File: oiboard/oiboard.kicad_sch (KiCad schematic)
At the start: 37 parts, among them J1 Conn_01x04, U1 LM324

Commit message: feat: finalize the board layout
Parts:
- removed D?: (no value), symbol LED:WS2812
- added D1, D10, D11, D12, D13, D14, D15, D16, D2, D3, D4, D5, D6, D7, D8, D9: APA102, LED_SMD:LED_RGB_5050-6, symbol LED:APA102
- added TP1, TP10, TP11, TP12, TP13, TP2, TP3, TP4, TP5, TP6, TP7, TP8, TP9: TestPoint, TestPoint:TestPoint_THTPad_D1.5mm_Drill0.7mm, symbol Connector:TestPoint
- D17: renamed from D?; value (none) -> LED; footprint (none) -> LED_THT:LED_D5.0mm
- D18, D19, D20: renamed from D?; footprint (none) -> LED_THT:LED_D5.0mm
- Q1: renamed from Q?; value (none) -> 2N3904; footprint (none) -> Package_TO_SOT_THT:TO-92_Inline
- R1: footprint Resistor_THT:R_Axial_DIN0207_L6.3mm_D2.5mm_P15.24mm_Horizontal -> Resistor_THT:R_Axial_DIN0207_L6.3mm_D2.5mm_P10.16mm_Horizontal
- R10, R8, R9: renamed from R?; value R -> 10k; footprint (none) -> Resistor_THT:R_Axial_DIN0207_L6.3mm_D2.5mm_P10.16mm_Horizontal
- R11, R12, R13, R15, R2, R3, R4, R5, R6, R7: renamed from R?; footprint Resistor_THT:R_Axial_DIN0207_L6.3mm_D2.5mm_P15.24mm_Horizontal -> Resistor_THT:R_Axial_DIN0207_L6.3mm_D2.5mm_P10.16mm_Horizontal
- R14: renamed from R?; footprint Resistor_THT:R_Axial_DIN0207_L6.3mm_D2.5mm_P15.24mm_Horizontal -> Button_Switch_THT:SW_CuK_JS202011CQN_DPDT_Straight
- SW1: renamed from SW?; footprint (none) -> Button_Switch_THT:SW_PUSH_6mm
- SW2: renamed from SW?; footprint (none) -> Button_Switch_THT:SW_DIP_SPSTx03_Slide_9.78x9.8mm_W7.62mm_P2.54mm
- gave numbers to parts that had none: 10
- renumbered J1 to J3
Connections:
- net GND is gone; now on net +5V: A1.29 (GND), A1.4 (GND), J1.1 (Pin_1), J1.4 (Pin_4), J2.1 (Pin_1), J2.4 (Pin_4), J3.1 (Pin_1), J4.1 (Pin_1), J5.1 (Pin_1), J7.1 (Pin_1), Q1.1 (E), Q2.1 (E), Q3.1 (E), Q4.1 (E), R10.2, R11.2, R2.1, R4.2, R6.2, R8.2, R9.2, SW1.1, U1.11 (V-)
- net +5V: now also D1.3 (GND), D1.4 (VCC), D10.3 (GND), D10.4 (VCC), D11.3 (GND), D11.4 (VCC), D12.3 (GND), D12.4 (VCC), D13.3 (GND), D13.4 (VCC), D14.3 (GND), D14.4 (VCC), D15.3 (GND), D15.4 (VCC), D16.3 (GND), D16.4 (VCC), D2.3 (GND), D2.4 (VCC), D3.3 (GND), D3.4 (VCC), D4.3 (GND), D4.4 (VCC), D5.3 (GND), D5.4 (VCC), D6.3 (GND), D6.4 (VCC), D7.3 (GND), D7.4 (VCC), D8.3 (GND), D8.4 (VCC), D9.3 (GND), D9.4 (VCC)
- net led_a: now also TP10.1
- net led_b: now also TP11.1
- net led_c: now also TP12.1
- net led_d: now also TP13.1
- net sensor_a: now also TP1.1
- net sensor_b: now also TP2.1
- net sensor_c: now also TP3.1
- net sensor_d: now also TP9.1
- net sw3: now reaches R10.1, SW2.4
- net sw3: now also A1.21 (A2), TP7.1
- net led_data: now reaches A1.10 (D7)
- net led_data: now also D8.1 (DI), TP6.1
- net led_clock : now reaches A1.11 (D8)
- net led_clock : now also D8.2 (CI), TP8.1
- net sw1: now reaches A1.19 (A0)
- net sw1: now also R8.1, SW2.6, TP4.1
- net sw2: now reaches A1.20 (A1)
- net sw2: now also R9.1, SW2.5, TP5.1
- new net: D12.6 (DO), D13.1 (DI)
- new net: D12.5 (CO), D13.2 (CI)
- new net: D13.5 (CO), D14.2 (CI)
- new net: D13.6 (DO), D14.1 (DI)
- new net: D6.1 (DI), D7.6 (DO)
- new net: D6.2 (CI), D7.5 (CO)
- new net: D5.2 (CI), D6.5 (CO)
- new net: D5.1 (DI), D6.6 (DO)
- new net: D14.6 (DO), D15.1 (DI)
- new net: D14.5 (CO), D15.2 (CI)
- new net: D15.5 (CO), D16.2 (CI)
- new net: D15.6 (DO), D16.1 (DI)
- new net: D7.2 (CI), D8.5 (CO)
- new net: D7.1 (DI), D8.6 (DO)
- new net: D11.6 (DO), D12.1 (DI)
- new net: D11.5 (CO), D12.2 (CI)
- new net: D1.6 (DO), D9.1 (DI)
- new net: D1.5 (CO), D9.2 (CI)
- new net: D10.2 (CI), D9.5 (CO)
- new net: D10.1 (DI), D9.6 (DO)
- new net: D2.1 (DI), D3.6 (DO)
- new net: D2.2 (CI), D3.5 (CO)
- new net: D1.2 (CI), D2.5 (CO)
- new net: D1.1 (DI), D2.6 (DO)
- new net: D4.1 (DI), D5.6 (DO)
- new net: D4.2 (CI), D5.5 (CO)
- new net: D3.2 (CI), D4.5 (CO)
- new net: D3.1 (DI), D4.6 (DO)
- new net: D10.6 (DO), D11.1 (DI)
- new net: D10.5 (CO), D11.2 (CI)
- no-connect marks 5 -> 11
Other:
- moved on the sheet: A1, D17, D18, D19, D20, J3, J4, J5, J6, J7, Q1, Q2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

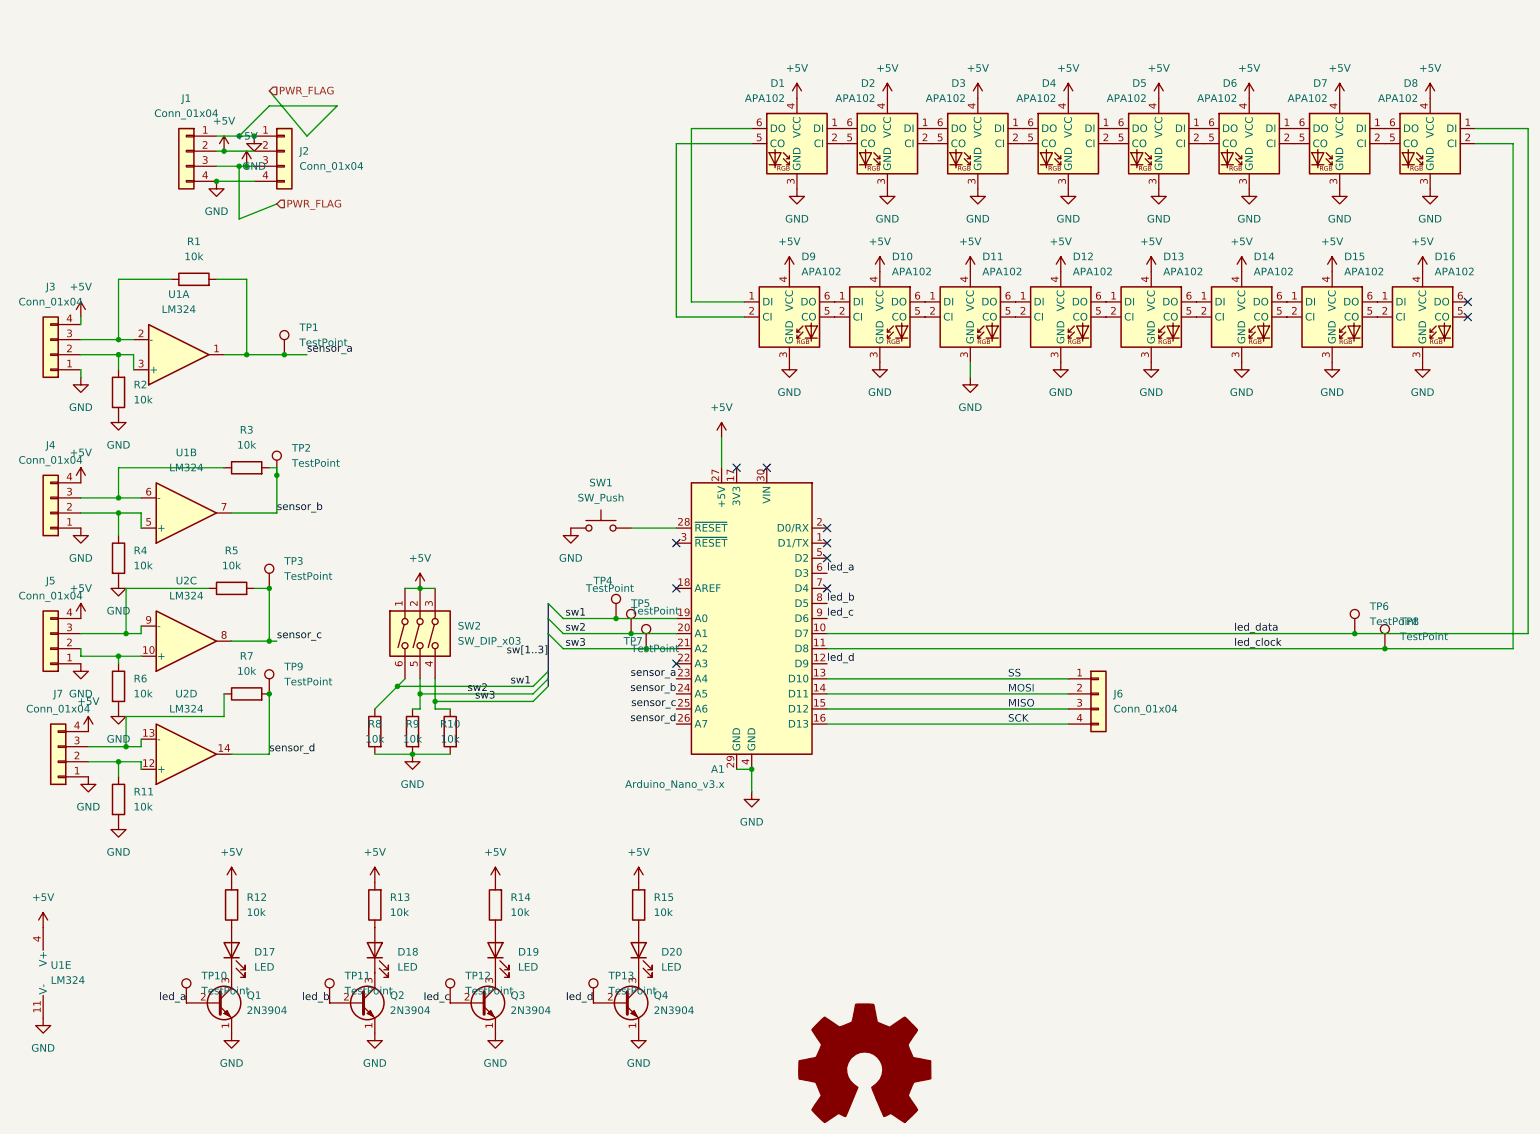
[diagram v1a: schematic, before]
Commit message: add premlimarp PCB layout
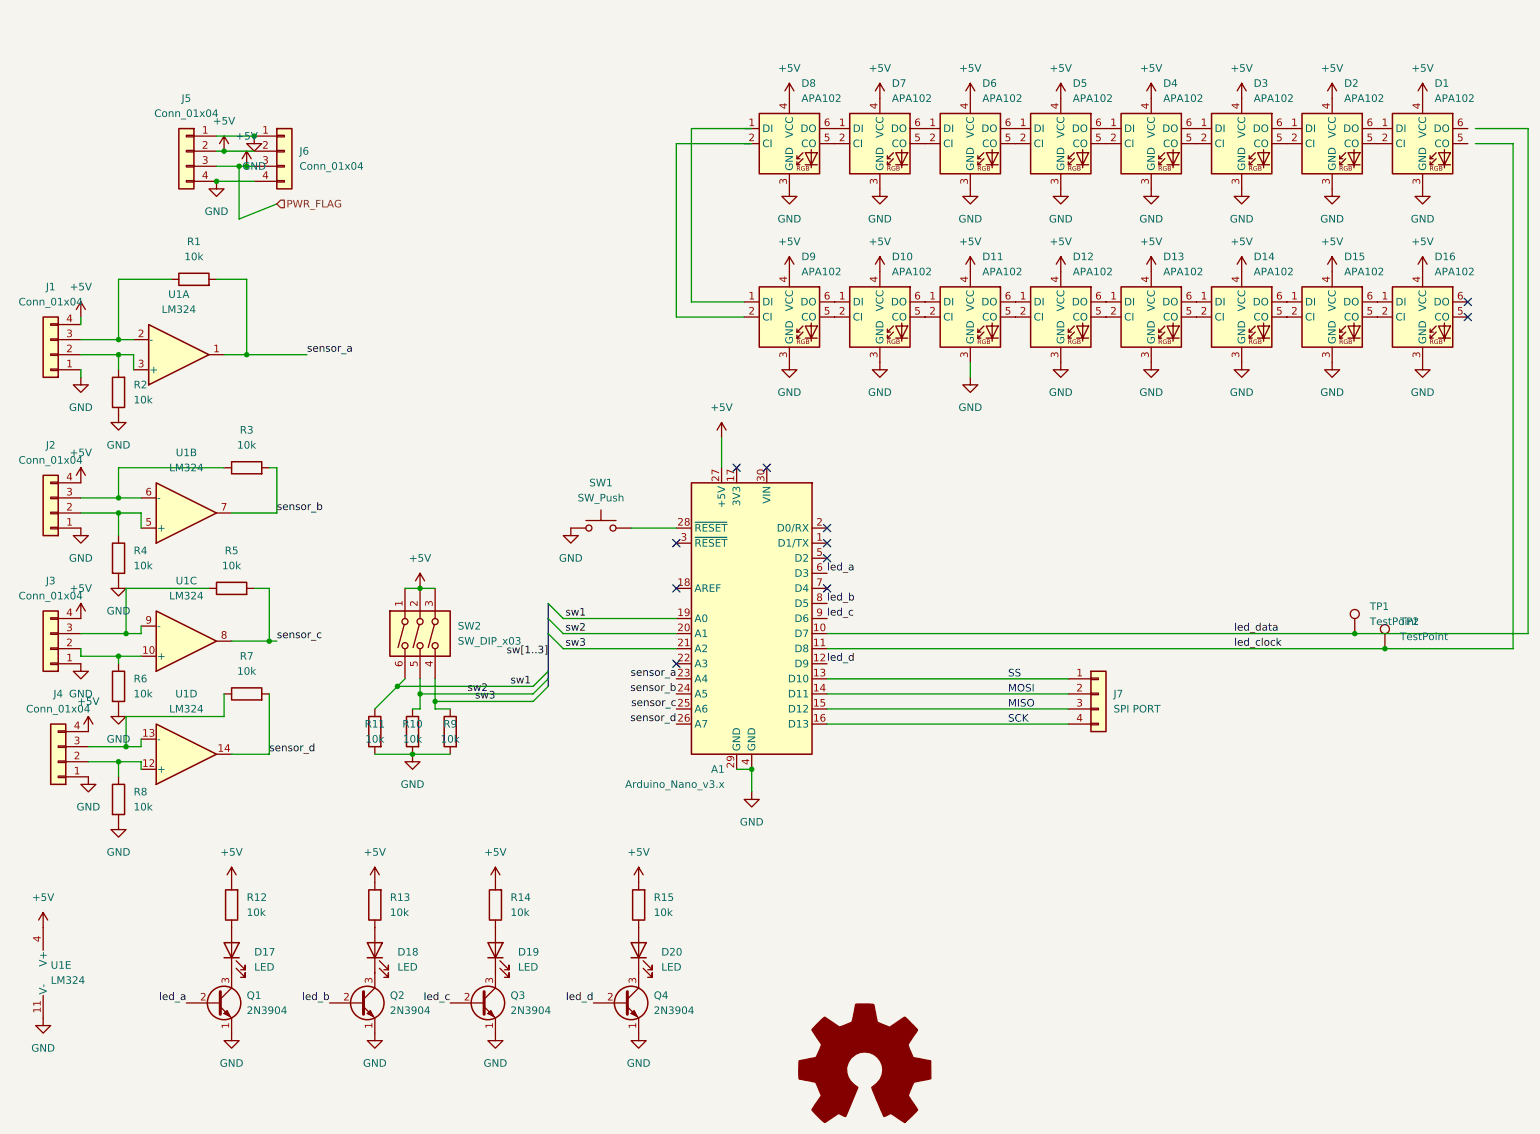
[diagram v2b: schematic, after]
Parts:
- removed TP1, TP10, TP11, TP12, TP13, TP2, TP3, TP4, TP5, TP7, TP9: TestPoint, TestPoint:TestPoint_THTPad_D1.5mm_Drill0.7mm, symbol Connector:TestPoint
- J7: renamed from J6; value Conn_01x04 -> SPI PORT; footprint TerminalBlock:TerminalBlock_bornier-4_P5.08mm -> Connector_PinHeader_2.54mm:PinHeader_1x04_P2.54mm_Horizontal
- R14: footprint Button_Switch_THT:SW_CuK_JS202011CQN_DPDT_Straight -> Resistor_THT:R_Axial_DIN0207_L6.3mm_D2.5mm_P10.16mm_Horizontal
- renumbered J3 to J1, J4 to J2, J5 to J3, J7 to J4, J1 to J5, J2 to J6, R9 to R10, R8 to R11, R11 to R8, R10 to R9, TP6 to TP1, TP8 to TP2, U2 to U1
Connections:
- net +5V: no longer A1.29 (GND), A1.4 (GND), D1.3 (GND), D10.3 (GND), D11.3 (GND), D12.3 (GND), D13.3 (GND), D14.3 (GND), D15.3 (GND), D16.3 (GND), D2.3 (GND), D3.3 (GND), D4.3 (GND), D5.3 (GND), D6.3 (GND), D7.3 (GND), D8.3 (GND), D9.3 (GND), J1.1 (Pin_1), J2.1 (Pin_1), J3.1 (Pin_1), J4.1 (Pin_1), J5.1 (Pin_1), J5.4 (Pin_4), J6.1 (Pin_1), J6.4 (Pin_4), Q1.1 (E), Q2.1 (E), Q3.1 (E), Q4.1 (E), R10.2, R11.2, R2.1, R4.2, R6.2, R8.2, R9.2, SW1.1, U1.11 (V-)
- net led_clock : no longer D8.2 (CI)
- net led_data: no longer D8.1 (DI)
- net at D9.1 (DI): no longer D1.6 (DO)
- net at D9.2 (CI): no longer D1.5 (CO)
- new net GND: A1.29 (GND), A1.4 (GND), D1.3 (GND), D10.3 (GND), D11.3 (GND), D12.3 (GND), D13.3 (GND), D14.3 (GND), D15.3 (GND), D16.3 (GND), D2.3 (GND), D3.3 (GND), D4.3 (GND), D5.3 (GND), D6.3 (GND), D7.3 (GND), D8.3 (GND), D9.3 (GND), J1.1 (Pin_1), J2.1 (Pin_1), J3.1 (Pin_1), J4.1 (Pin_1), J5.1 (Pin_1), J5.4 (Pin_4), J6.1 (Pin_1), J6.4 (Pin_4), Q1.1 (E), Q2.1 (E), Q3.1 (E), Q4.1 (E), R10.2, R11.2, R2.1, R4.2, R6.2, R8.2, R9.2, SW1.1, U1.11 (V-)
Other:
- moved on the sheet: D1, D2, D3, D4, D5, D6, D7, D8

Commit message: finalize pcb design 0.0
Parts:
- removed TP1, TP2: TestPoint, TestPoint:TestPoint_THTPad_D1.5mm_Drill0.7mm, symbol Connector:TestPoint
- added H1, H2, H3, H4: (no value), symbol Mechanical:MountingHole
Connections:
- net led_clock : now also D1.5 (CO)
- net led_data: now also D1.6 (DO)
- net sensor_b: now also A1.26 (A7); no longer A1.24 (A5)
- net sensor_c: now also A1.24 (A5), U1.14; no longer A1.25 (A6), U1.8
- net sensor_d: now also A1.25 (A6), U1.8; no longer A1.26 (A7), U1.14
- net at R3.1, U1.6 (-): now also J4.3 (Pin_3); no longer J2.3 (Pin_3)
- net at J3.2 (Pin_2), U1.10 (+): now also R8.1; no longer R6.1
- net at R4.1, U1.5 (+): now also J4.2 (Pin_2); no longer J2.2 (Pin_2)
- net at R1.1, U1.2 (-): now also J2.3 (Pin_3); no longer J1.3 (Pin_3)
- net at D8.1 (DI): now also D9.1 (DI)
- net at D8.2 (CI): now also D9.2 (CI)
- net at R2.2, U1.3 (+): now also J2.2 (Pin_2); no longer J1.2 (Pin_2)
- net at J3.3 (Pin_3), U1.9 (-): now also R7.1; no longer R5.1
- new net: J1.2 (Pin_2), R6.1, U1.12 (+)
- new net: J1.3 (Pin_3), R5.1, U1.13 (-)
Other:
- moved on the sheet: J1, J2, J3, J4, J7, U1C, U1D

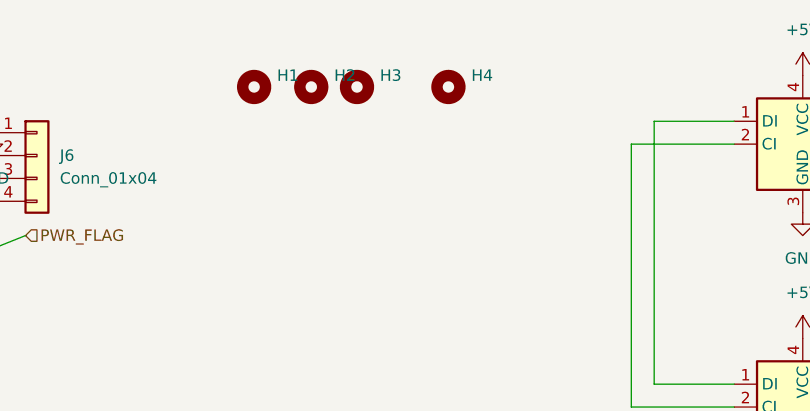
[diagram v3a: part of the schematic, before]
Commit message: add logo to board
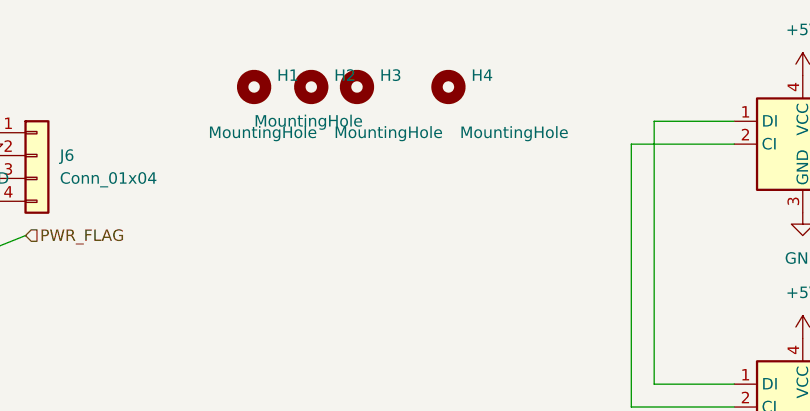
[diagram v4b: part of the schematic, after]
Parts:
- H1, H2, H3, H4: value (none) -> MountingHole; footprint (none) -> MountingHole:MountingHole_3mm
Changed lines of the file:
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@@
       (effects (font (size 1.27 1.27)) (justify left))
     )
-    (property "Value" "" (id 1) (at 88.9 26.67 0)
-      (effects (font (size 1.27 1.27)) (justify left))
-    )
-    (property "Footprint" "" (id 2) (at 95.25 22.86 0)
+    (property "Value" "MountingHole" (id 1) (at 88.9 26.67 0)
+      (effects (font (size 1.27 1.27)) (justify left))
+    )
+    (property "Footprint" "MountingHole:MountingHole_3mm" (id 2) (at 95.25 22.86 0)
       (effects (font (size 1.27 1.27)) hide)
     )
@@
       (effects (font (size 1.27 1.27)) (justify left))
     )
-    (property "Value" "" (id 1) (at 83.82 27.94 0)
-      (effects (font (size 1.27 1.27)) (justify left))
-    )
-    (property "Footprint" "" (id 2) (at 88.9 22.86 0)
+    (property "Value" "MountingHole" (id 1) (at 83.82 27.94 0)
+      (effects (font (size 1.27 1.27)) (justify left))
+    )
+    (property "Footprint" "MountingHole:MountingHole_3mm" (id 2) (at 88.9 22.86 0)
       (effects (font (size 1.27 1.27)) hide)
     )
@@
       (effects (font (size 1.27 1.27)) (justify left))
     )
-    (property "Value" "" (id 1) (at 97.79 27.94 0)
-      (effects (font (size 1.27 1.27)) (justify left))
-    )
-    (property "Footprint" "" (id 2) (at 100.33 22.86 0)
+    (property "Value" "MountingHole" (id 1) (at 97.79 27.94 0)
+      (effects (font (size 1.27 1.27)) (justify left))
+    )
+    (property "Footprint" "MountingHole:MountingHole_3mm" (id 2) (at 100.33 22.86 0)
       (effects (font (size 1.27 1.27)) hide)
     )
@@
       (effects (font (size 1.27 1.27)) (justify left))
     )
-    (property "Value" "" (id 1) (at 111.76 27.94 0)
-      (effects (font (size 1.27 1.27)) (justify left))
-    )
-    (property "Footprint" "" (id 2) (at 110.49 22.86 0)
-      (effects (font (size 1.27 1.27)) hide)
-    )
+    (property "Value" "MountingHole" (id 1) (at 111.76 27.94 0)
+      (effects (font (size 1.27 1.27)) (justify left))
+    )
+    (property "Footprint" "MountingHole:MountingHole_3mm" (id 2) (at 110.49 22.86 0)
+      (effects (font (size 1.27 1.27)) hide)
+    )

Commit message: comment
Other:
- note added: "This is the daughterboard which performs lights and input"
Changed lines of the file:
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@@
+    (effects (font (size 1.27 1.27)) (justify left bottom))
+  )
+  (text "This is the daughterboard which performs lights and input"
+    (at 180.34 170.18 0)
     (effects (font (size 1.27 1.27)) (justify left bottom))
   )

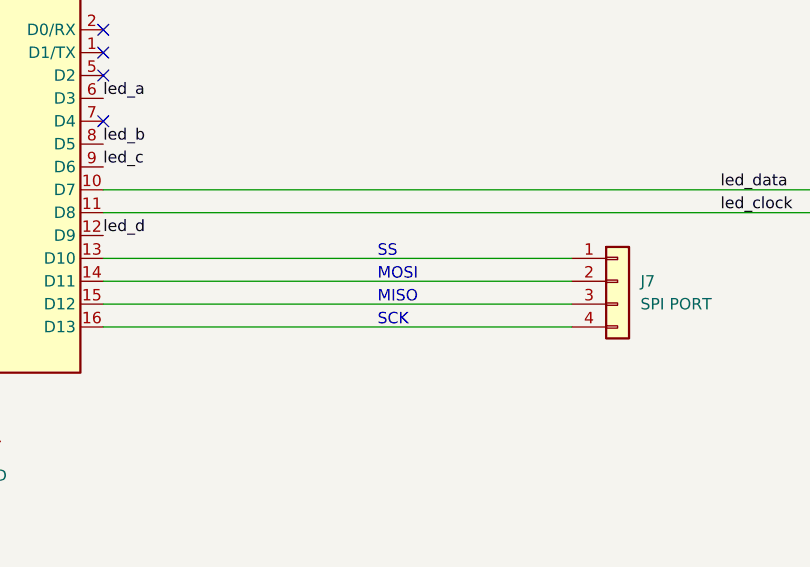
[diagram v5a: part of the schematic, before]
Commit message: add additional labels to the daughter oiboard
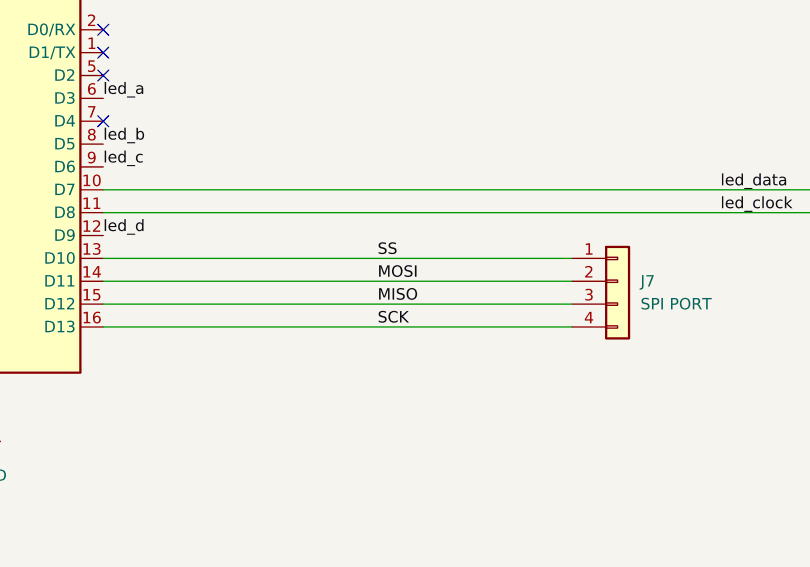
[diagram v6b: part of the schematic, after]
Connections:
- net SS: now reaches A1.13 (D10), J7.1 (Pin_1)
- net MOSI: now reaches A1.14 (D11), J7.2 (Pin_2)
- net MISO: now reaches A1.15 (D12), J7.3 (Pin_3)
- net SCK: now reaches A1.16 (D13), J7.4 (Pin_4)
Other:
- note removed: "MISO"
- note removed: "MOSI"
- note removed: "SCK"
- note removed: "SS"
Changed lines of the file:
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@@
     (stroke (width 0) (type default) (color 0 0 0 0))
-  )
-  (text "MISO" (at 186.69 124.46 0)
-    (effects (font (size 1.27 1.27)) (justify left bottom))
-  )
-  (text "MOSI" (at 186.69 121.92 0)
-    (effects (font (size 1.27 1.27)) (justify left bottom))
   )
   (text "This is the daughterboard which performs lights and input"
@@
     (effects (font (size 1.27 1.27)) (justify left bottom))
   )
-  (text "SCK" (at 186.69 127 0)
-    (effects (font (size 1.27 1.27)) (justify left bottom))
-  )
-  (text "SS" (at 186.69 119.38 0)
-    (effects (font (size 1.27 1.27)) (justify left bottom))
-  )
   (label "sensor_b" (at 130.81 127 180)
     (effects (font (size 1.27 1.27)) (justify right bottom))
+  )
+  (label "MOSI" (at 186.69 121.92 0)
+    (effects (font (size 1.27 1.27)) (justify left bottom))
   )
   (label "sensor_c" (at 63.5 113.03 0)
@@
     (effects (font (size 1.27 1.27)) (justify left bottom))
   )
+  (label "MISO" (at 186.69 124.46 0)
+    (effects (font (size 1.27 1.27)) (justify left bottom))
+  )
   (label "led_d" (at 156.21 116.84 0)
     (effects (font (size 1.27 1.27)) (justify left bottom))
@@
     (effects (font (size 1.27 1.27)) (justify left bottom))
   )
+  (label "SCK" (at 186.69 127 0)
+    (effects (font (size 1.27 1.27)) (justify left bottom))
+  )
   (label "sensor_a" (at 130.81 119.38 180)
     (effects (font (size 1.27 1.27)) (justify right bottom))
@@
     (effects (font (size 1.27 1.27)) (justify right bottom))
   )
+  (label "SS" (at 186.69 119.38 0)
+    (effects (font (size 1.27 1.27)) (justify left bottom))
+  )
   (label "led_d" (at 116.84 173.99 180)
